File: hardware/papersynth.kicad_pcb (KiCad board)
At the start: 2 copper layers, 200 x 75 mm, 102 parts, among them J1 USB_OTG, J2 JACK_2P, J3 Micro_SD_Card_Det, J4 JACK_TRS_5PINS, J5 JACK_2P, Q1 Q_NPN_BEC, Q2 Q_NPN_BEC, SW1 SW_Push, SW2 SW_Push, U1 CP2102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

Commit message: Routed LED drivers
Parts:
- added C40: 10uF, Capacitors_SMD:C_0603, F.Cu at (202.0, 101.8)
- added C41: 100uF, Capacitors_SMD:CP_Elec_5x5.3, F.Cu at (220.6, 98.0)
- added C42: 10uF, Capacitors_SMD:C_0603, F.Cu at (211.8, 111.6)
- added R33: 10k, Resistors_SMD:R_0603, F.Cu at (217.4, 109.4)
- BT1: value Battery -> Battery_Cell
- C37: value C -> 10uF
- C38, C39: value C -> 0.1uF
- R16: value 5.1k -> 2k
- U10: value 8x8_LED_MATRIX_RGB -> PCA9745B; footprint PaperSynth:8x8_RGB_RED_MATRIX -> PaperSynth:HTSSOP-28_4.4x9.7mm_Pitch0.65mm_SmallThermalPad
- U7: value TLC5947 -> 8x8_LED_MATRIX_RG; footprint Housings_DFN_QFN:QFN-32-1EP_5x5mm_Pitch0.5mm -> PaperSynth:8x8_RG_LED_MATRIX
- moved C17 87.0 mm to (216.7, 44.4)
- moved C18 87.0 mm to (216.7, 46.2)
- moved C19 87.0 mm to (225.6, 41.4)
- moved C20 87.0 mm to (227.2, 41.4)
- moved C21 87.0 mm to (219.3, 41.4)
- moved C22 87.0 mm to (228.2, 44.7)
- moved C27 87.0 mm to (217.8, 41.4)
- moved C28 87.0 mm to (228.2, 46.2)
- moved C29 87.0 mm to (216.7, 47.7)
- moved C30 87.0 mm to (216.7, 49.2)
- moved C31 87.0 mm to (211.9, 44.4)
- moved C32 87.0 mm to (204.3, 36.8)
- moved C33 87.0 mm to (208.4, 46.4)
- moved C34 87.0 mm to (206.6, 46.4)
- moved C35 87.0 mm to (216.5, 31.7)
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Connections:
- LS1 pad 2: Net-(J4-Pad5) -> Net-(LS1-Pad2)
- R16 pad 1: GND -> Net-(R16-Pad1)
- R16 pad 2: Net-(R16-Pad2) -> GND
- R30 pad 1: Net-(J4-Pad4) -> Net-(R30-Pad1)
- R31 pad 1: Net-(J4-Pad4) -> Net-(R30-Pad1)
- U10 pad 1: Net-(U10-Pad1) -> Net-(R16-Pad1)
- U10 pad 10: Net-(U10-Pad10) -> GND
- U10 pad 11: Net-(U10-Pad11) -> /LED_DISPLAY/K7G
- U10 pad 12: Net-(U10-Pad12) -> /LED_DISPLAY/K7R
- U10 pad 13: Net-(U10-Pad13) -> /LED_DISPLAY/K8G
- U10 pad 14: Net-(U10-Pad14) -> /LED_DISPLAY/K8R
- U10 pad 15: Net-(U10-Pad15) -> /LED_DISPLAY/K4R
- U10 pad 16: Net-(U10-Pad16) -> /LED_DISPLAY/K4G
- U10 pad 17: Net-(U10-Pad17) -> /LED_DISPLAY/K3R
- U10 pad 18: Net-(U10-Pad18) -> /LED_DISPLAY/K3G
- U10 pad 19: Net-(U10-Pad19) -> GND
- U10 pad 2: Net-(U10-Pad2) -> GND
- U10 pad 20: Net-(U10-Pad20) -> /LED_DISPLAY/K2R
- U10 pad 21: Net-(U10-Pad21) -> /LED_DISPLAY/K2G
- U10 pad 22: Net-(U10-Pad22) -> /LED_DISPLAY/K1R
- U10 pad 23: Net-(U10-Pad23) -> /LED_DISPLAY/K1G
- U10 pad 24: Net-(U10-Pad24) -> GND
- U10 pad 25: Net-(U10-Pad25) -> Net-(R33-Pad1)
- U10 pad 26: Net-(U10-Pad26) -> /ESP32_MODULE/COL_C
- U10 pad 27: Net-(U10-Pad27) -> /ESP32_MODULE/COL_D
- U10 pad 28: Net-(U10-Pad28) -> +3V3
- U10 pad 29: Net-(U10-Pad29) -> GND
- U10 pad 4: Net-(U10-Pad4) -> /ESP32_MODULE/COL_LAT
- U10 pad 5: Net-(U10-Pad5) -> /ESP32_MODULE/COL_OE
- U10 pad 6: Net-(U10-Pad6) -> /LED_DISPLAY/K5G
- U10 pad 7: Net-(U10-Pad7) -> /LED_DISPLAY/K5R
- U10 pad 8: Net-(U10-Pad8) -> /LED_DISPLAY/K6G
- U10 pad 9: Net-(U10-Pad9) -> /LED_DISPLAY/K6R
- U7 pad 1: Net-(U10-Pad9) -> /LED_DISPLAY/K5G
- U7 pad 10: Net-(U10-Pad27) -> /LED_DISPLAY/K8G
- U7 pad 11: Net-(U10-Pad26) -> /LED_DISPLAY/K8R
- U7 pad 12: Net-(U10-Pad25) -> Net-(U7-Pad12)
- U7 pad 13: Net-(U10-Pad24) -> Net-(U7-Pad13)
- U7 pad 14: Net-(U10-Pad23) -> /LED_DISPLAY/K4R
- U7 pad 15: Net-(U10-Pad22) -> /LED_DISPLAY/K4G
- U7 pad 16: Net-(U10-Pad21) -> Net-(U7-Pad16)
- U7 pad 17: Net-(U10-Pad1) -> /LED_DISPLAY/K3R
- U7 pad 18: Net-(U10-Pad2) -> /LED_DISPLAY/K3G
- U7 pad 19: Net-(U10-Pad3) -> Net-(U7-Pad19)
- U7 pad 2: Net-(U10-Pad10) -> /LED_DISPLAY/K5R
- U7 pad 20: Net-(U10-Pad4) -> /LED_DISPLAY/K2R
- U7 pad 21: Net-(U10-Pad5) -> /LED_DISPLAY/K2G
- U7 pad 22: Net-(U10-Pad6) -> Net-(U7-Pad22)
- U7 pad 23: Net-(U10-Pad7) -> /LED_DISPLAY/K1R
- U7 pad 24: Net-(U10-Pad8) -> /LED_DISPLAY/K1G
- U7 pad 3: Net-(U10-Pad11) -> Net-(U7-Pad3)
- U7 pad 4: Net-(U10-Pad12) -> /LED_DISPLAY/K6G
- U7 pad 5: Net-(U10-Pad13) -> /LED_DISPLAY/K6R
- U7 pad 6: Net-(U10-Pad14) -> Net-(U7-Pad6)
- U7 pad 7: Net-(U10-Pad15) -> /LED_DISPLAY/K7G
- U7 pad 8: Net-(U10-Pad16) -> /LED_DISPLAY/K7R
- U7 pad 9: Net-(U10-Pad28) -> Net-(U7-Pad9)
- U9 pad 10: Net-(U10-Pad30) -> Net-(U7-Pad6)
- U9 pad 11: Net-(U10-Pad31) -> Net-(U7-Pad9)
- U9 pad 12: Net-(U10-Pad32) -> Net-(U7-Pad12)
- U9 pad 5: Net-(U10-Pad17) -> Net-(U7-Pad22)
- U9 pad 6: Net-(U10-Pad18) -> Net-(U7-Pad19)
- U9 pad 7: Net-(U10-Pad19) -> Net-(U7-Pad16)
- U9 pad 8: Net-(U10-Pad20) -> Net-(U7-Pad13)
- U9 pad 9: Net-(U10-Pad29) -> Net-(U7-Pad3)
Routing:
- net Net-(U10-Pad17): track 70.4 -> 0.00 mm, vias 2 -> 0
- net Net-(U10-Pad18): track 67.6 -> 0.00 mm, vias 2 -> 0
- net Net-(U10-Pad19): track 64.5 -> 0.00 mm, vias 2 -> 0
- net Net-(U10-Pad20): track 62.9 -> 0.00 mm, vias 2 -> 0
- net Net-(U10-Pad16): track 62.8 -> 0.00 mm
- net Net-(U10-Pad15): track 59.8 -> 0.00 mm
- net Net-(U10-Pad21): track 58.6 -> 0.00 mm, vias 1 -> 0
- net Net-(U10-Pad14): track 56.9 -> 0.00 mm
- net Net-(U10-Pad22): track 56.8 -> 0.00 mm, vias 1 -> 0
- net Net-(U10-Pad23): track 55.4 -> 0.00 mm, vias 1 -> 0
- net Net-(U7-Pad13): track 0.00 -> 54.6 mm, vias 0 -> 1
- net Net-(U7-Pad12): track 0.00 -> 54.6 mm, vias 0 -> 1
- net Net-(U10-Pad24): track 54.1 -> 0.00 mm, vias 1 -> 0
- net Net-(U10-Pad13): track 53.9 -> 0.00 mm
- net Net-(U10-Pad25): track 53.3 -> 0.00 mm, vias 1 -> 0
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- removed copper zone on B.Cu, net GND
- removed copper zone on F.Cu, net GND
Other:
- board size 200 x 75 mm -> 200 x 50 mm

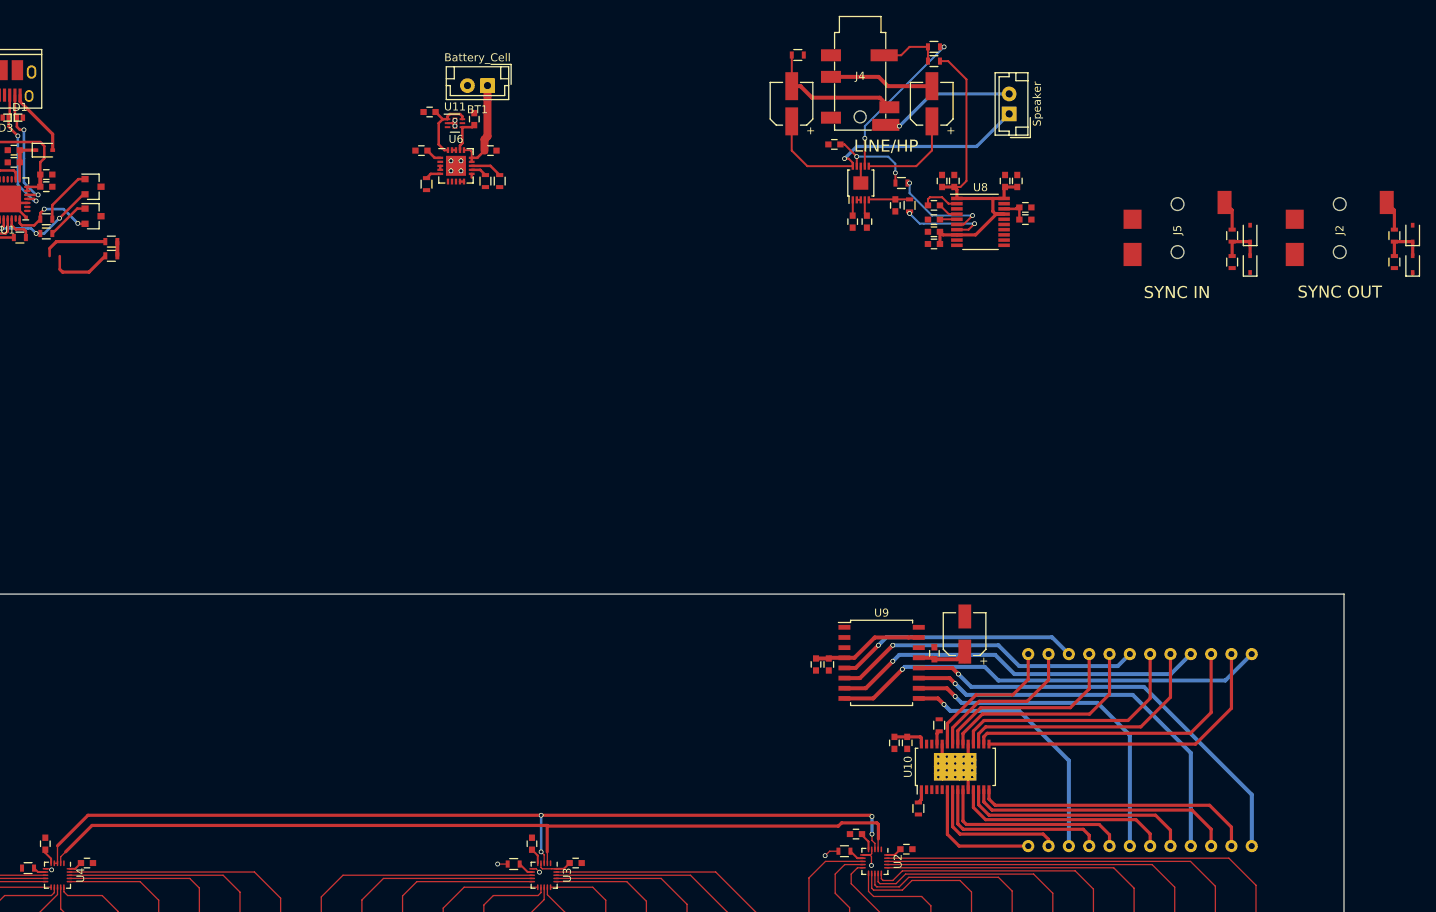
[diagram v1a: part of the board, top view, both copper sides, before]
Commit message: Routed audio out
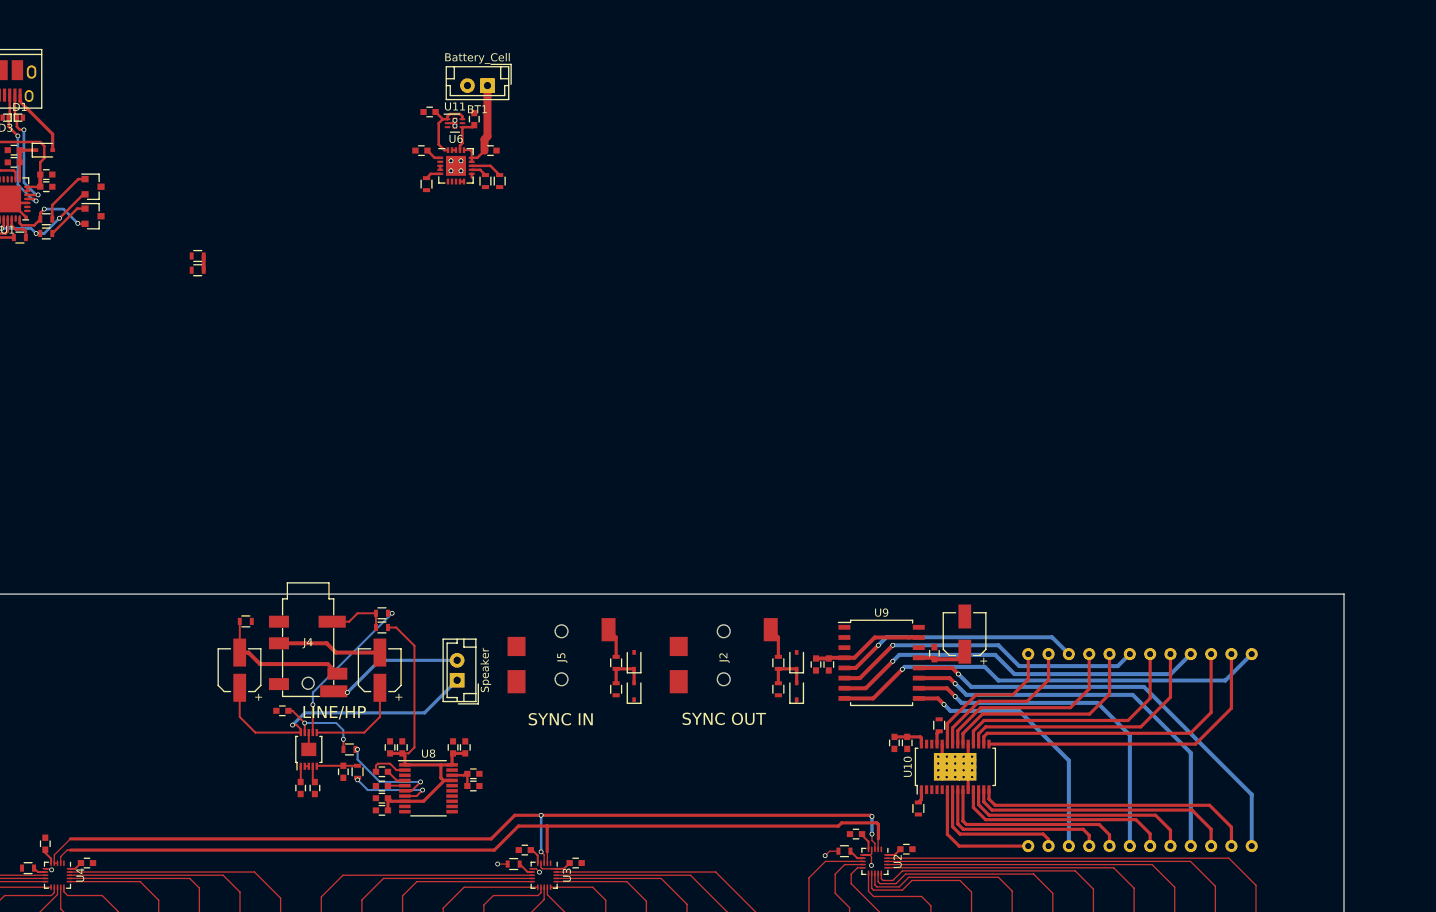
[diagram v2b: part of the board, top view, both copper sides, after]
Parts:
- moved C17 98.9 mm to (147.7, 115.2)
- moved C19 98.9 mm to (156.6, 112.2)
- moved C20 98.9 mm to (158.2, 112.2)
- moved C21 98.9 mm to (150.3, 112.2)
- moved C27 98.9 mm to (148.8, 112.2)
- moved C31 98.9 mm to (142.9, 115.2)
- moved R28 98.9 mm to (144.7, 115.2)
- moved R29 98.9 mm to (143.7, 112.4)
- moved R30 98.9 mm to (147.7, 95.4)
- moved U13 98.9 mm to (138.6, 112.4)
- moved U8 98.9 mm to (153.6, 117.3)
- moved C18 98.9 mm to (147.7, 117.0)
- moved C22 98.9 mm to (159.2, 115.5)
- moved C28 98.9 mm to (159.2, 117.0)
- moved C29 98.9 mm to (147.7, 118.5)
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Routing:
- net /ESP32_MODULE/SDA: track 124.8 -> 116.2 mm
- net /ESP32_MODULE/SCL: track 121.0 -> 112.6 mm

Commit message: Routed USB adapter
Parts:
- BT1: value Battery_Cell -> BAT
- moved C23 90.5 mm to (118.0, 109.1)
- moved J3 90.5 mm to (119.3, 101.9)
- moved R17 90.5 mm to (114.8, 111.1)
- moved R18 90.5 mm to (113.8, 109.3)
- moved R19 90.5 mm to (123.4, 109.1)
- moved R20 90.5 mm to (122.4, 111.1)
- moved R21 90.5 mm to (127.0, 97.4)
- moved C5 74.6 mm to (110.0, 111.7), turned to 270 degrees
- moved C3 73.5 mm to (105.2, 114.1), turned to 270 degrees
- moved C6 72.9 mm to (108.4, 111.7), turned to 270 degrees
- moved R27 71.5 mm to (109.0, 109.3), turned to 0 degrees
- moved C4 71.0 mm to (106.8, 113.1), turned to 270 degrees
- moved D1 69.7 mm to (106.2, 103.0)
- moved D3 69.6 mm to (103.0, 103.0)
- moved J1 68.9 mm to (104.2, 98.0)
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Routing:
- net CMD: track 0.00 -> 44.3 mm
- net DAT2: track 2.29 -> 46.4 mm
- net SDCLK: track 0.00 -> 42.9 mm
- net DAT3: track 4.52 -> 45.6 mm
- net /ESP32_MODULE/SCL: track 112.6 -> 153.5 mm, vias 0 -> 2
- net /ESP32_MODULE/SDA: track 116.2 -> 155.3 mm, vias 4 -> 6
- net DAT0: track 4.36 -> 42.8 mm
- net DAT1: track 2.60 -> 41.0 mm
- net /ESP32_MODULE/U0TXD: track 7.84 -> 32.1 mm, vias 0 -> 2
- net /ESP32_MODULE/U0RXD: track 5.27 -> 28.2 mm, vias 0 -> 2
- net RTS: track 18.8 -> 9.42 mm, vias 3 -> 0
- net /ESP32_MODULE/EN: track 7.68 -> 14.7 mm
- net +5V: track 6.16 -> 12.6 mm
- net Net-(Q2-Pad1): track 5.38 -> 10.5 mm, vias 0 -> 2
- net Net-(D2-Pad2): track 8.57 -> 4.36 mm
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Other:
- board size 200 x 50 mm -> 200 x 48.5 mm

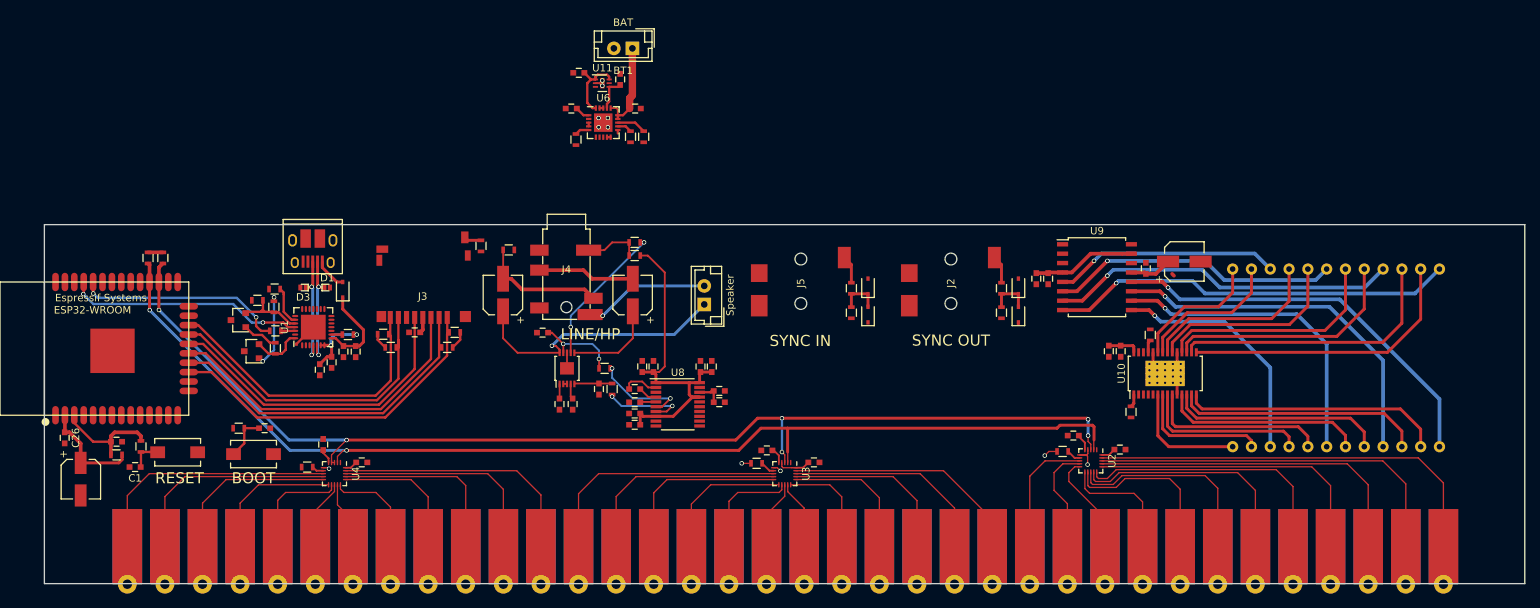
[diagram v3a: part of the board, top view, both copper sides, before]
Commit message: Routed power management
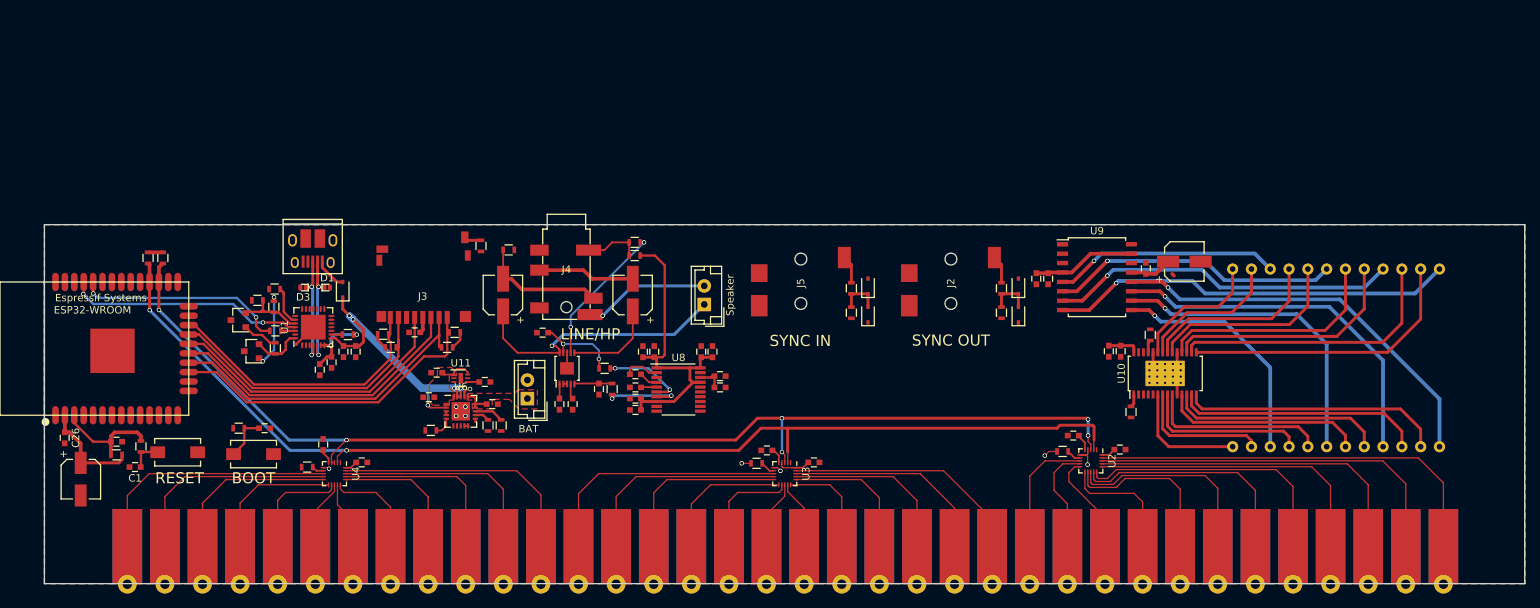
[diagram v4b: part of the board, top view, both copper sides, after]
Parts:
- moved BT1 49.4 mm to (133.2, 118.0), turned to 90 degrees
- moved C15 44.8 mm to (121.0, 114.5)
- moved C16 44.8 mm to (127.5, 115.8), turned to 0 degrees
- moved C14 44.4 mm to (128.5, 118.8)
- moved U11 44.2 mm to (124.2, 115.2)
- moved R13 43.9 mm to (120.2, 122.3), turned to 0 degrees
- moved R14 43.5 mm to (127.9, 121.6)
- moved C13 43.5 mm to (119.9, 117.8)
- moved R15 43.5 mm to (129.7, 121.6)
- moved U6 43.5 mm to (124.2, 119.7)
- moved C19 2.00 mm to (156.7, 111.7)
- moved C20 2.00 mm to (158.3, 111.7)
- moved C27 2.00 mm to (148.9, 111.7)
- moved C17 2.00 mm to (147.8, 114.7)
- moved C18 2.00 mm to (147.8, 116.5)
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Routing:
- net +5V: track 12.6 -> 39.0 mm, vias 0 -> 5
- net +BATT: track 12.6 -> 3.87 mm
- net VUNREG: track 17.2 -> 10.6 mm
- net CMD: track 44.3 -> 40.9 mm
- net SDCLK: track 42.9 -> 39.7 mm
- net DAT0: track 42.8 -> 39.7 mm
- net DAT1: track 41.0 -> 38.0 mm
- net +3V3: track 110.4 -> 107.7 mm, vias 2 -> 3
- net GND: track 30.0 -> 27.7 mm, vias 11 -> 9
- net DAT2: track 46.4 -> 44.5 mm
- net Net-(R29-Pad2): track 13.0 -> 11.2 mm
- net DAT3: track 45.6 -> 44.0 mm
- net Net-(R28-Pad2): track 11.4 -> 10.8 mm
- net Net-(R13-Pad2): track 1.94 -> 2.57 mm
- added copper zone on F.Cu, net +BATT
- added copper zone on B.Cu, net GND
- added copper zone on F.Cu, net GND
- added copper zone on F.Cu, net VUNREG

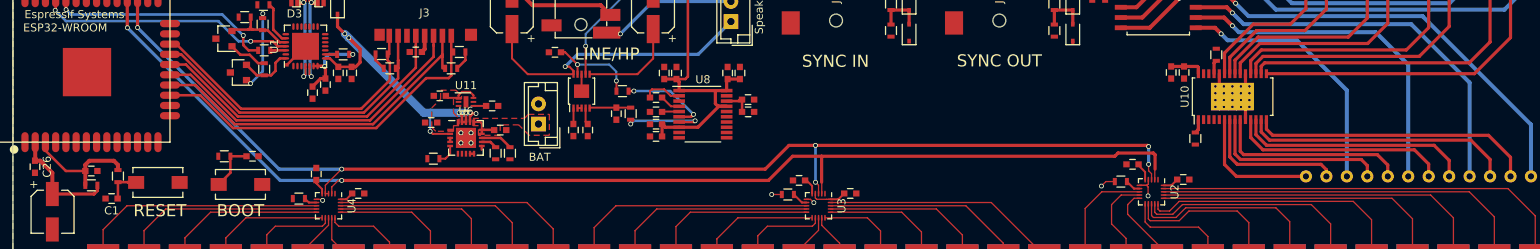
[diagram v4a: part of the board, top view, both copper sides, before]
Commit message: Fixed library problems and re-generated netlist
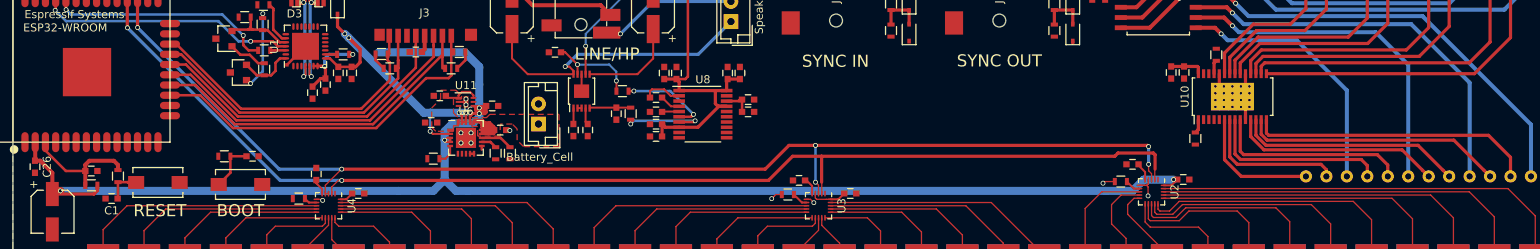
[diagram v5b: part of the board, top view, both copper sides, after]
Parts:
- BT1: value BAT -> Battery_Cell
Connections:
- LS1 pad 2: Net-(LS1-Pad2) -> Net-(J4-Pad5)
- R30 pad 1: Net-(R30-Pad1) -> Net-(J4-Pad4)
- R31 pad 1: Net-(R30-Pad1) -> Net-(J4-Pad4)
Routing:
- net +3V3: track 107.7 -> 287.6 mm, vias 3 -> 7
- net +BATT: track 3.87 -> 15.1 mm
- net Net-(LS1-Pad2): track 9.69 -> 0.00 mm
- net Net-(J4-Pad5): track 7.46 -> 17.2 mm
- net Net-(R30-Pad1): track 4.08 -> 0.00 mm
- net Net-(J4-Pad4): track 3.61 -> 7.68 mm
- net GND: track 27.7 -> 30.3 mm, vias 9 -> 12
- net /LED_DISPLAY/K7R: track 29.2 -> 28.1 mm
- net /LED_DISPLAY/K8G: track 33.5 -> 32.4 mm
- net /LED_DISPLAY/K7G: track 27.2 -> 26.2 mm

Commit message: Finished routing
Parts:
- moved R1 44.5 mm to (117.4, 125.9), turned to 90 degrees
- moved R2 40.8 mm to (115.4, 125.0), turned to 90 degrees
- moved C32 9.11 mm to (144.4, 109.5), turned to 90 degrees
- moved R20 6.56 mm to (117.0, 114.8), turned to 135 degrees
- moved C17 5.83 mm to (150.8, 109.7)
- moved C18 5.83 mm to (150.8, 111.5)
- moved C19 5.83 mm to (159.7, 106.7)
- moved C20 5.83 mm to (161.3, 106.7)
- moved C21 5.83 mm to (153.4, 106.7)
- moved C22 5.83 mm to (162.3, 110.0)
- moved C27 5.83 mm to (151.9, 106.7)
- moved C28 5.83 mm to (162.3, 111.5)
- moved C29 5.83 mm to (150.8, 113.0)
- moved C30 5.83 mm to (150.8, 114.5)
- moved U8 5.83 mm to (156.7, 111.8)
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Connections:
- U12 pad 10: /AUDIO_INTERFACE/LRCLK -> /ESP32_MODULE/SYNC_OUT
- U12 pad 11: /AUDIO_INTERFACE/BCLK -> /ESP32_MODULE/SYNC_IN
- U12 pad 12: Net-(U12-Pad12) -> /AUDIO_INTERFACE/LRCLK
- U12 pad 13: /ESP32_MODULE/SYNC_OUT -> /AUDIO_INTERFACE/DACDAT
- U12 pad 14: /ESP32_MODULE/SYNC_IN -> /AUDIO_INTERFACE/BCLK
- U12 pad 36: /AUDIO_INTERFACE/DACDAT -> Net-(U12-Pad36)
- U12 pad 6: /ESP32_MODULE/COL_C -> /ESP32_MODULE/COL_OE
- U12 pad 7: /ESP32_MODULE/COL_D -> /ESP32_MODULE/COL_LAT
- U12 pad 8: /ESP32_MODULE/COL_LAT -> /ESP32_MODULE/COL_C
- U12 pad 9: /ESP32_MODULE/COL_OE -> /ESP32_MODULE/COL_D
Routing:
- net GND: track 30.3 -> 260.4 mm, vias 12 -> 36
- net /ESP32_MODULE/COL_OE: track 0.00 -> 150.9 mm, vias 0 -> 4
- net /ESP32_MODULE/COL_LAT: track 0.00 -> 148.3 mm, vias 0 -> 4
- net /ESP32_MODULE/COL_C: track 0.00 -> 146.2 mm, vias 0 -> 2
- net /ESP32_MODULE/COL_D: track 0.00 -> 143.9 mm, vias 0 -> 2
- net /ESP32_MODULE/ROW_D: track 0.00 -> 132.1 mm, vias 0 -> 2
- net VUNREG: track 10.6 -> 142.3 mm, vias 0 -> 3
- net /ESP32_MODULE/ROW_C: track 0.00 -> 130.6 mm, vias 0 -> 2
- net /ESP32_MODULE/SYNC_OUT: track 0.00 -> 125.2 mm, vias 0 -> 2
- net +3V3: track 287.6 -> 402.7 mm, vias 7 -> 22
- net /ESP32_MODULE/SYNC_IN: track 0.00 -> 103.3 mm, vias 0 -> 2
- net /AUDIO_INTERFACE/LRCLK: track 0.00 -> 92.3 mm, vias 0 -> 2
- net /AUDIO_INTERFACE/DACDAT: track 0.00 -> 88.1 mm, vias 0 -> 2
- net /AUDIO_INTERFACE/BCLK: track 0.00 -> 85.6 mm, vias 0 -> 2
- net CARDET: track 2.35 -> 47.8 mm
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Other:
- board text removed: "LINE/HP"
